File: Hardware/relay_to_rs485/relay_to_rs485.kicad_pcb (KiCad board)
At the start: 2 copper layers, 90 x 56 mm, 51 parts, among them J1 Relay Inputs A to E connected, J2 RS485 Output Screw Terminal, J3 Screw_Terminal_InputGrounds, J4 Jack-DC, J5 UART OUT, Q1 IRLML6401, U1 ESP32-S3-WROOM-1, U2 MAX485E, U3 SMX1117MP-3.3

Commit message: v2.0.1
Board layout improvements
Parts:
- J4: value Jack-DC -> Max 12VDC IN
- moved TP15 20.5 mm to (114.8, 95.2), turned to 180 degrees
- moved J4 9.25 mm to (95.4, 86.7)
- moved C5 6.41 mm to (107.7, 85.3), turned to 90 degrees
- moved C4 2.71 mm to (104.8, 85.3), turned to 90 degrees
- moved TP14 0.85 mm to (93.8, 74.0)
- moved L1 0.20 mm to (123.5, 83.2)
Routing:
- net VCC: track 20.2 -> 23.1 mm

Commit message: update
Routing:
- net /InputH: track 31.6 -> 31.0 mm
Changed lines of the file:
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@@
 		(tags "test point SMD pad rectangle square")
 		(property "Reference" "TP15"
-			(at 0 -1.648 360)
+			(at 0 -1.648 0)
 			(layer "F.SilkS")
 			(hide yes)
@@
 		)
 		(property "Value" "~"
-			(at 0 1.75 360)
+			(at 0 1.75 0)
 			(layer "F.Fab")
 			(hide yes)
@@
 		)
 		(fp_text user "TP_VCC"
-			(at 0 -2.3 360)
+			(at 0 -2.3 0)
 			(layer "F.SilkS")
 			(effects
@@
 		(tags "THT Terminal Block Xinya XY308-2.54-2P pitch 2.54mm size 5.58x6.5mm^2 drill 1.2mm pad 2mm")
 		(property "Reference" "J4"
-			(at 5.5 0 360)
+			(at 5.5 0 0)
 			(layer "F.SilkS" knockout)
 			(hide yes)
@@
 	)
 	(segment
-		(start 121.58 107.2)
-		(end 133.55 107.2)
+		(start 121.5 114)
+		(end 121.5 109.72)
 		(width 0.2)
 		(layer "F.Cu")
@@
 	)
 	(segment
-		(start 121.5 114)
-		(end 121.5 109.72)
+		(start 132.395 107.2)
+		(end 121.58 107.2)
 		(width 0.2)
 		(layer "F.Cu")
@@
 	)
 	(segment
-		(start 120.28 108.5)
-		(end 121.58 107.2)
+		(start 140.425 98.22)
+		(end 140.425 99.17)
 		(width 0.2)
 		(layer "F.Cu")
@@
 	)
 	(segment
-		(start 133.55 107.2)
-		(end 140.425 100.325)
+		(start 121.58 107.2)
+		(end 120.28 108.5)
 		(width 0.2)
 		(layer "F.Cu")
@@
 	)
 	(segment
-		(start 140.425 100.325)
-		(end 140.425 98.22)
+		(start 140.425 99.17)
+		(end 132.395 107.2)
 		(width 0.2)
 		(layer "F.Cu")
@@
 	)
 	(zone
-		(net 44)
-		(net_name "/InputH")
-		(layer "F.Cu")
-		(name "$teardrop_padvia$")
-		(hatch full 0.1)
-		(priority 30078)
-		(attr
-			(teardrop
-				(type padvia)
-			)
-		)
-		(connect_pads yes
-			(clearance 0)
-		)
-		(min_thickness 0.0254)
-		(filled_areas_thickness no)
-		(fill yes
-			(thermal_gap 0.5)
-			(thermal_bridge_width 0.5)
-			(island_removal_mode 1)
-			(island_area_min 10)
-		)
-		(polygon
-			(pts
-				(xy 140.325 99.42) (xy 140.525 99.42) (xy 140.875 98.97) (xy 140.425 98.219) (xy 139.975 98.97)
-			)
-		)
-	)
-	(zone
 		(net 42)
 		(net_name "/InputF")
@@
 	)
 	(zone
+		(net 44)
+		(net_name "/InputH")
+		(layer "F.Cu")
+		(name "$teardrop_padvia$")
+		(hatch full 0.1)
+		(priority 30001)
+		(attr
+			(teardrop
+				(type padvia)
+			)
+		)
+		(connect_pads yes
+			(clearance 0)
+		)
+		(min_thickness 0.0254)
+		(filled_areas_thickness no)
+		(fill yes
+			(thermal_gap 0.5)
+			(thermal_bridge_width 0.5)
+			(island_removal_mode 1)
+			(island_area_min 10)
+		)
+		(polygon
+			(pts
+				(xy 140.177513 99.276066) (xy 140.318934 99.417487) (xy 140.763076 98.97) (xy 140.425707 98.219293)
+				(xy 139.975 98.97)
+			)
+		)
+	)
+	(zone
 		(net 3)
 		(net_name "/A")
@@
 	)
 	(zone
-		(net 44)
-		(net_name "/InputH")
-		(layer "F.Cu")
-		(name "$teardrop_padvia$")
-		(hatch full 0.1)
-		(priority 30023)
-		(attr
-			(teardrop
-				(type padvia)
-			)
-		)
-		(connect_pads yes
-			(clearance 0)
-		)
-		(min_thickness 0.0254)
-		(filled_areas_thickness no)
-		(fill yes
-			(thermal_gap 0.5)
-			(thermal_bridge_width 0.5)
-			(island_removal_mode 1)
-			(island_area_min 10)
-		)
-		(polygon
-			(pts
-				(xy 121.4 109.99466) (xy 121.6 109.99466) (xy 121.20388 108.117317) (xy 120.28 108.499) (xy 119.897317 109.42388)
-			)
-		)
-	)
-	(zone
 		(net 4)
 		(net_name "/B")
@@
 	)
 	(zone
-		(net 44)
-		(net_name "/InputH")
-		(layer "F.Cu")
-		(name "$teardrop_padvia$")
-		(hatch full 0.1)
-		(priority 30021)
-		(attr
-			(teardrop
-				(type padvia)
-			)
-		)
-		(connect_pads yes
-			(clearance 0)
-		)
-		(min_thickness 0.0254)
-		(filled_areas_thickness no)
-		(fill yes
-			(thermal_gap 0.5)
-			(thermal_bridge_width 0.5)
-			(island_removal_mode 1)
-			(island_area_min 10)
-		)
-		(polygon
-			(pts
-				(xy 121.741523 107.3) (xy 121.741523 107.1) (xy 119.897317 107.57612) (xy 120.279 108.5) (xy 121.20388 108.882683)
-			)
-		)
-	)
-	(zone
 		(net 2)
 		(net_name "+3V3")
@@
 	)
 	(zone
+		(net 44)
+		(net_name "/InputH")
+		(layer "F.Cu")
+		(name "$teardrop_padvia$")
+		(hatch full 0.1)
+		(priority 30000)
+		(attr
+			(teardrop
+				(type padvia)
+			)
+		)
+		(connect_pads yes
+			(clearance 0)
+		)
+		(min_thickness 0.0254)
+		(filled_areas_thickness no)
+		(fill yes
+			(thermal_gap 0.5)
+			(thermal_bridge_width 0.5)
+			(island_removal_mode 1)
+			(island_area_min 10)
+		)
+		(polygon
+			(pts
+				(xy 121.4 109.99466) (xy 121.6 109.99466) (xy 121.20388 108.117317) (xy 120.28 108.499) (xy 119.897317 109.42388)
+			)
+		)
+	)
+	(zone
 		(net 38)
 		(net_name "/RX")
@@
 			)
 		)
+	)
+	(zone
+		(net 44)
+		(net_name "/InputH")
+		(layer "F.Cu")
+		(name "$teardrop_padvia$")
+		(hatch full 0.1)
+		(priority 30000)
+		(attr
+			(teardrop
+				(type padvia)
+			)
+		)
+		(connect_pads yes
+			(clearance 0)
+		)
+		(min_thickness 0.0254)
+		(filled_areas_thickness no)
+		(fill yes
+			(thermal_gap 0.5)
+			(thermal_bridge_width 0.5)
+			(island_removal_mode 1)
+			(island_area_min 10)
+		)
+		(polygon
+			(pts
+				(xy 121.741523 107.3) (xy 121.741523 107.1) (xy 119.897317 107.57612) (xy 120.279 108.5) (xy 121.20388 108.882683)
+			)
+		)

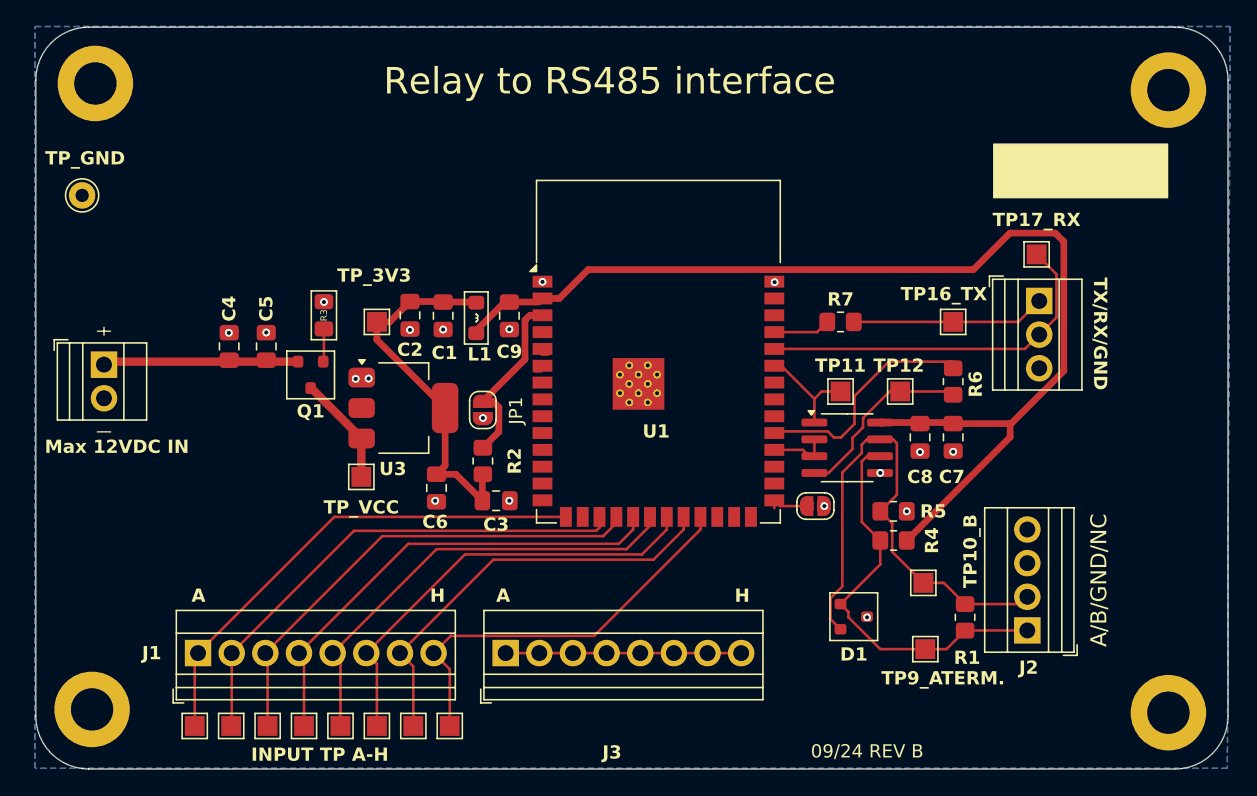
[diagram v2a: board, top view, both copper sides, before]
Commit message: Corrected reverse D-S pins for IRLM6401 Q1
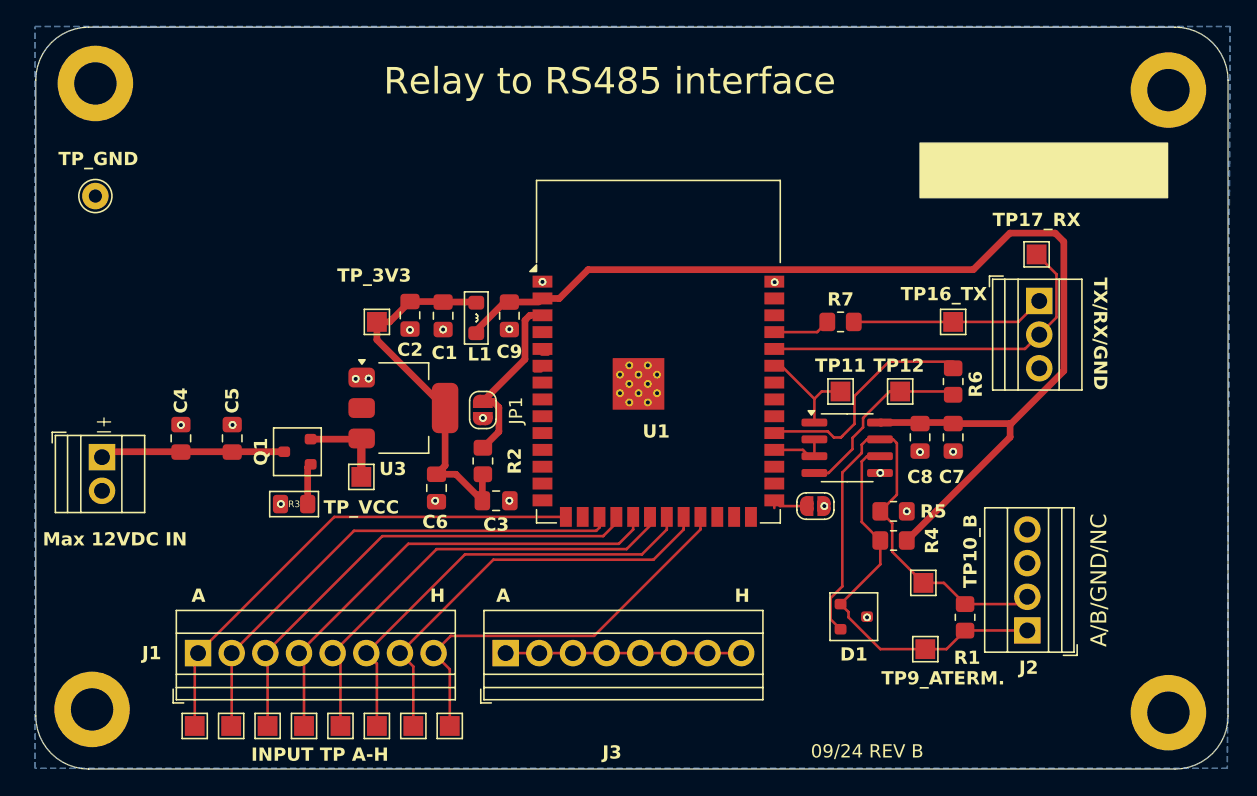
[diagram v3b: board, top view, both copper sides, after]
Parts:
- moved R3 14.4 mm to (109.8, 97.2), turned to 180 degrees
- moved C4 7.84 mm to (101.2, 92.3)
- moved C5 7.40 mm to (105.1, 92.3)
- moved J4 6.99 mm to (95.2, 93.7)
- moved Q1 5.89 mm to (110.0, 93.3), turned to 180 degrees
- moved TP14 1.00 mm to (94.8, 74.0)
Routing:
- net VCC: track 23.1 -> 20.7 mm
- net Net-(Q1-G): track 2.50 -> 3.09 mm

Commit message: More reworking of board
Addition of ZD1, MOSFET RP protection diode, reconfig of JP1 etc
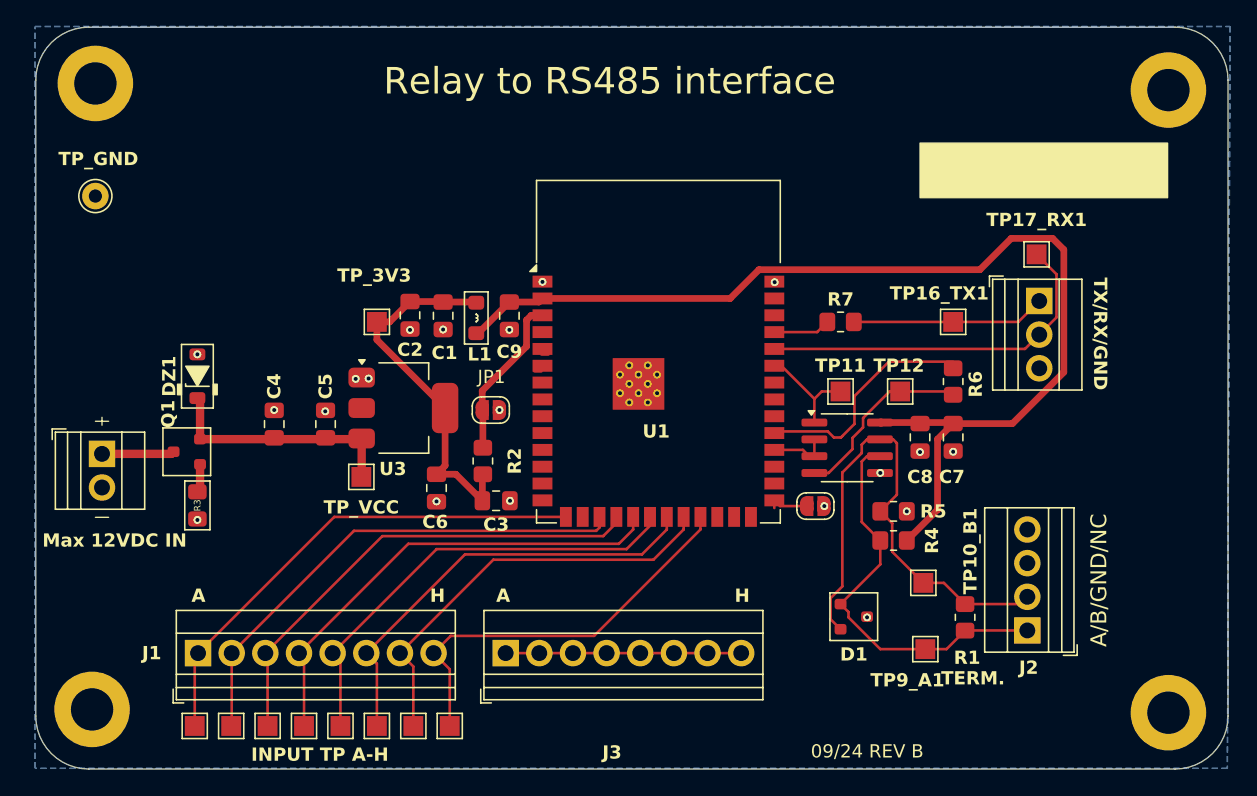
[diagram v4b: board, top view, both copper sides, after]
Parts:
- added DZ1: 7.5 or 8.2, PCM_Diode_SMD_Handsoldering_AKL:D_SOD-123_Zener, F.Cu at (102.5, 87.6)
- R3: value 10R -> 100R
- TP14_GND1: renamed from TP14; value TP_GND -> ~
- moved Q1 8.35 mm to (101.7, 93.3)
- moved R3 7.30 mm to (102.5, 97.3), turned to -90 degrees
- moved C4 7.13 mm to (108.2, 91.2)
- moved C5 7.13 mm to (112.1, 91.2)
- moved JP1 0.60 mm to (124.6, 90.2), turned to 0 degrees
- moved J4 0.25 mm to (95.2, 93.5)
- renumbered TP10_B to TP10_B1, TP13 to TP13_3V3, TP15 to TP15_VCC1, TP16_TX to TP16_TX1, TP17_RX to TP17_RX1, TP9_A to TP9_A1
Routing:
- net VCC: track 20.7 -> 24.6 mm
- net Net-(JP1-A): track 14.4 -> 12.4 mm
- net +3V3: track 114.5 -> 112.6 mm
- net Net-(Q1-G): track 3.09 -> 2.16 mm
- net GND: vias 19 -> 20

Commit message: More changes
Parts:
- R4, R5: value 680R -> 330R
- moved R6 11.8 mm to (150.6, 95.7), turned to 180 degrees
- moved R4 11.2 mm to (160.4, 109.8), turned to 90 degrees
- moved TP12 10.4 mm to (151.2, 98.2), turned to 90 degrees
- moved TP17_RX 9.96 mm to (159.4, 86.1), turned to 180 degrees
- moved R5 6.70 mm to (160.4, 101.8), turned to 90 degrees
- moved C7 5.72 mm to (165.2, 93.0)
- moved C8 5.72 mm to (162.7, 93.0)
- moved U2 5.72 mm to (157.2, 93.8)
- moved JP2 5.18 mm to (146.0, 101.5), turned to -90 degrees
- moved TP9_A 4.62 mm to (152.8, 109.0)
- moved TP10_B 4.43 mm to (152.9, 102.5)
- moved C4 1.60 mm to (109.8, 91.2)
- moved TP13_3V3 1.15 mm to (116.0, 82.3)
- moved J4 0.58 mm to (94.7, 93.4)
- moved R7 0.58 mm to (151.0, 84.1)
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- renumbered TP10_B1 to TP10_B, TP16_TX1 to TP16_TX, TP17_RX1 to TP17_RX, TP9_A1 to TP9_A
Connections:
- net /A renamed /A+
- net /B renamed /B-
- J4 pad 1: VCC -> Net-(Q1-D)
- Q1 pad 3: VCC -> Net-(Q1-D)
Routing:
- net Net-(U1-IO38): track 17.3 -> 6.03 mm
- net Net-(U1-IO37): track 4.49 -> 14.6 mm
- net +3V3: track 112.6 -> 122.6 mm
- net Net-(U2-DI): track 14.4 -> 5.81 mm
- net /RX: track 27.7 -> 20.4 mm
- net /B-: track 39.3 -> 32.7 mm
- net Net-(Q1-D): track 0.00 -> 6.58 mm
- net VCC: track 24.6 -> 18.7 mm
- net Net-(U1-IO42): track 8.05 -> 10.8 mm
- net Net-(JP2-A): track 3.21 -> 4.54 mm
- net /A+: track 31.9 -> 33.1 mm
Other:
- board text removed: "TERM."

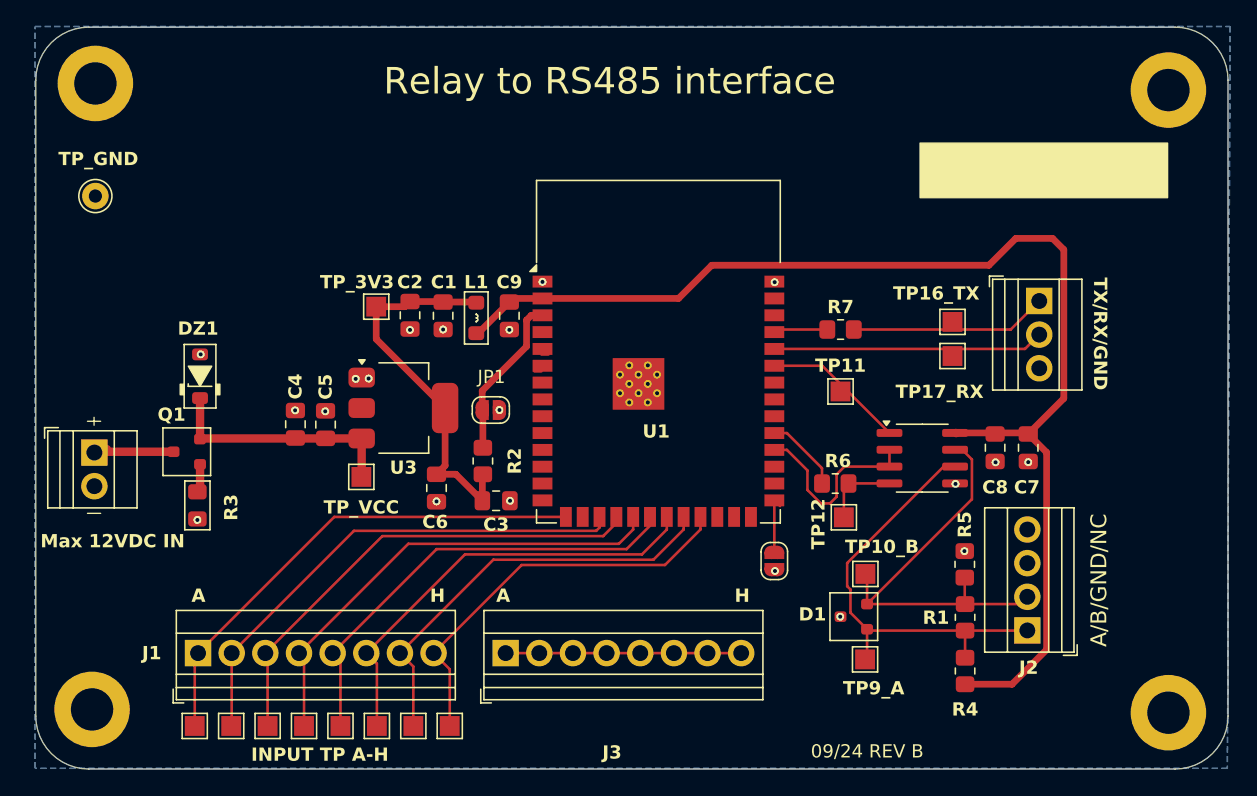
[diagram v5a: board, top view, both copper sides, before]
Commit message: Moved writing mark to back silkscreen
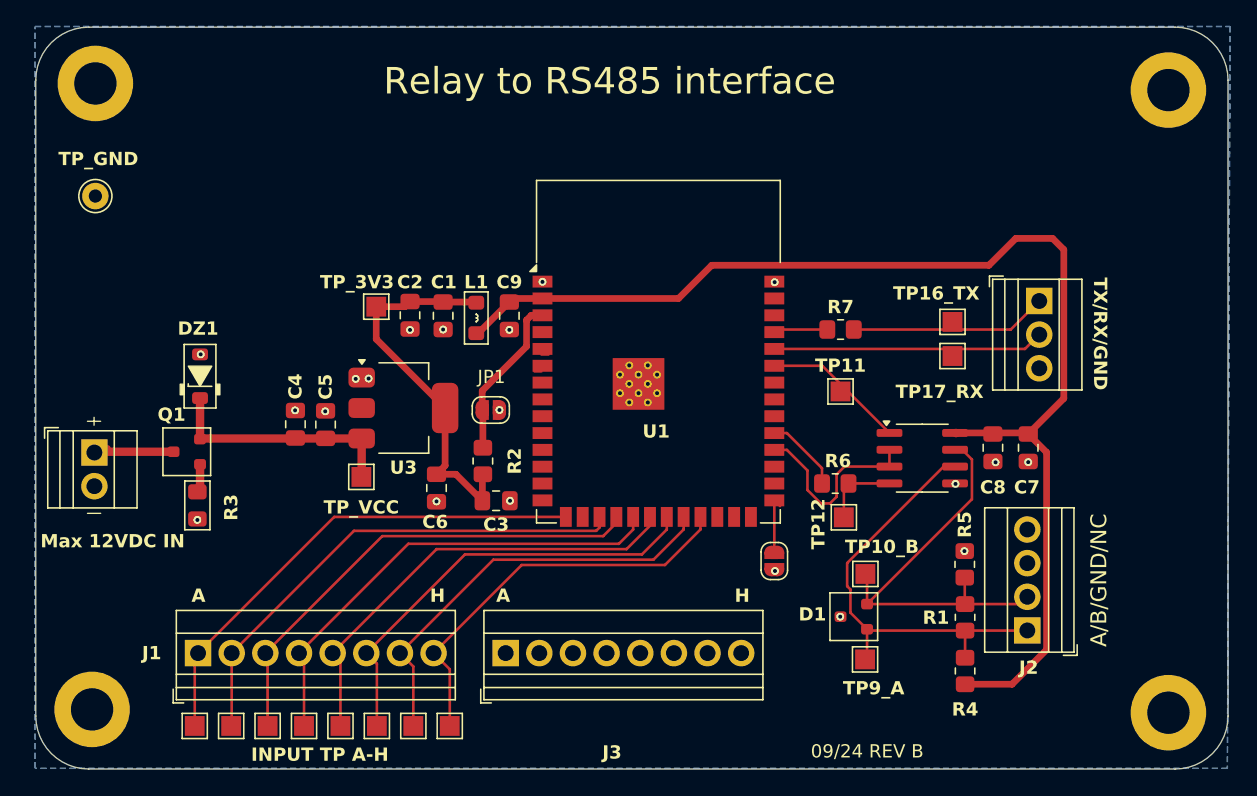
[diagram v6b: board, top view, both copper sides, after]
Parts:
- moved C8 0.17 mm to (162.5, 93.0)
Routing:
- net GND: track 17.8 -> 0.00 mm
